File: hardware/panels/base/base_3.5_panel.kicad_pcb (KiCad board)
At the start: 2 copper layers, 82.5 x 93 mm, 50 parts, among them IC1 single_pad_smd, IC2 single_pad_smd, J1 Conn 1, J2 Conn 2

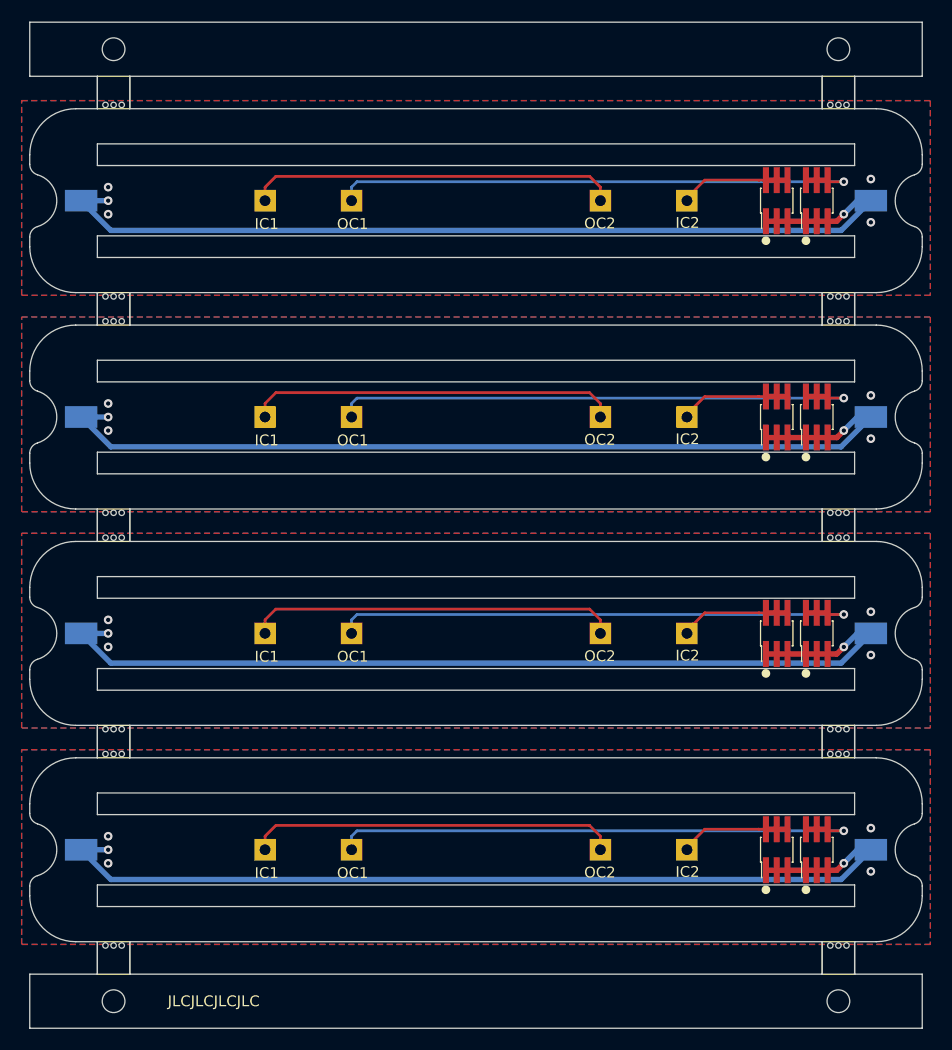
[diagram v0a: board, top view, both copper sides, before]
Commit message: Base PCB panels updates
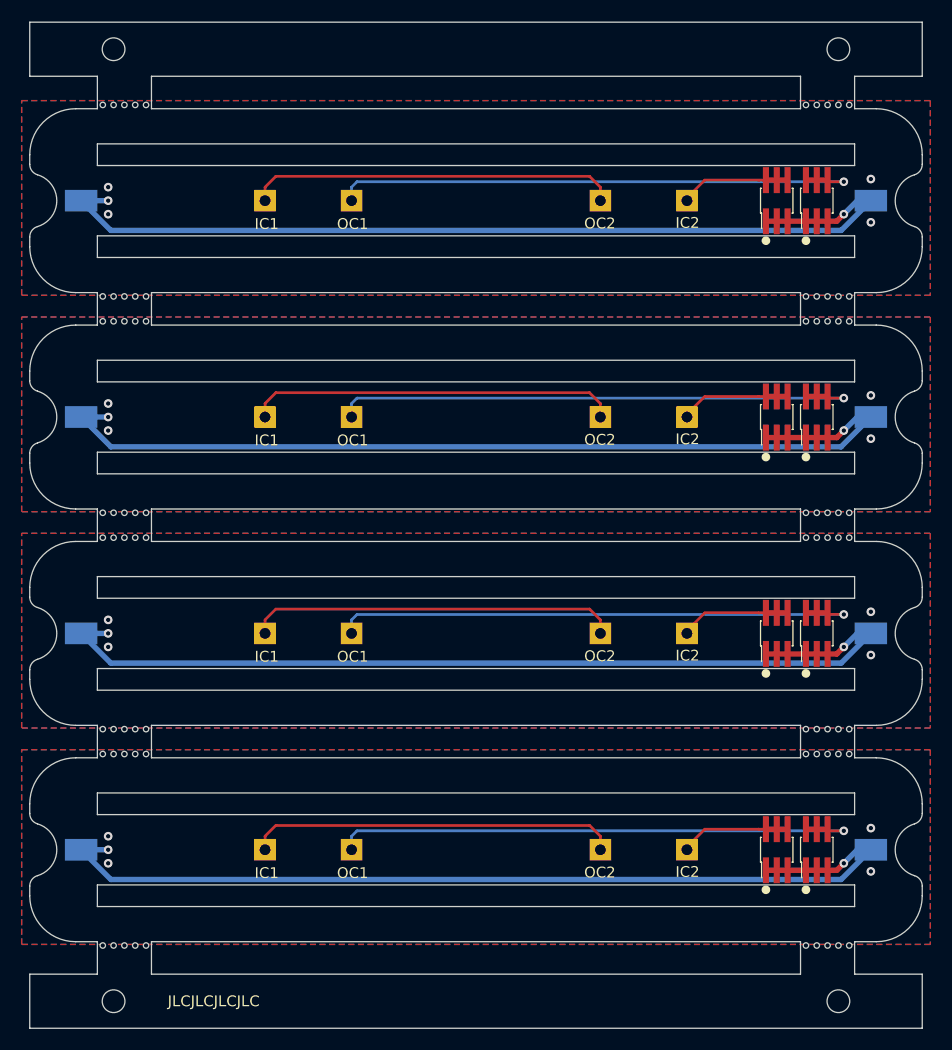
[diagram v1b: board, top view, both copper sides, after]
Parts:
- moved mouse-bite-3mm-slot 1.00 mm to (59.5, 129.2)
- moved mouse-bite-3mm-slot 1.00 mm to (59.5, 69.2)
- moved mouse-bite-3mm-slot 1.00 mm to (124.5, 129.2)
- moved mouse-bite-3mm-slot 1.00 mm to (124.5, 49.2)
- moved mouse-bite-3mm-slot 1.00 mm to (59.5, 49.2)
- moved mouse-bite-3mm-slot 1.00 mm to (124.5, 89.2)
- moved mouse-bite-3mm-slot 1.00 mm to (124.5, 109.2)
- moved mouse-bite-3mm-slot 1.00 mm to (59.5, 109.2)
- moved mouse-bite-3mm-slot 1.00 mm to (59.5, 89.2)
- moved mouse-bite-3mm-slot 1.00 mm to (124.5, 69.2)
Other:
- outline, holes or cut-outs redrawn
